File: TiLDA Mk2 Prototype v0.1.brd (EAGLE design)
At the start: 67.9 x 100 mm, 199 parts, among them IC1 ATSAM3X8EA-AU, IC10 MCP73831, IC2 MPU-6050, IC3 SRF-V1.2, IC5 S25FL216K0PMFI011, IC7 HMC5883LSMD (NP), IC8 MCP1825T-3302E/DC, IC9 TC1015-3V3, J1 ZX62-AB-5PA(11), J3 Arduino Headers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

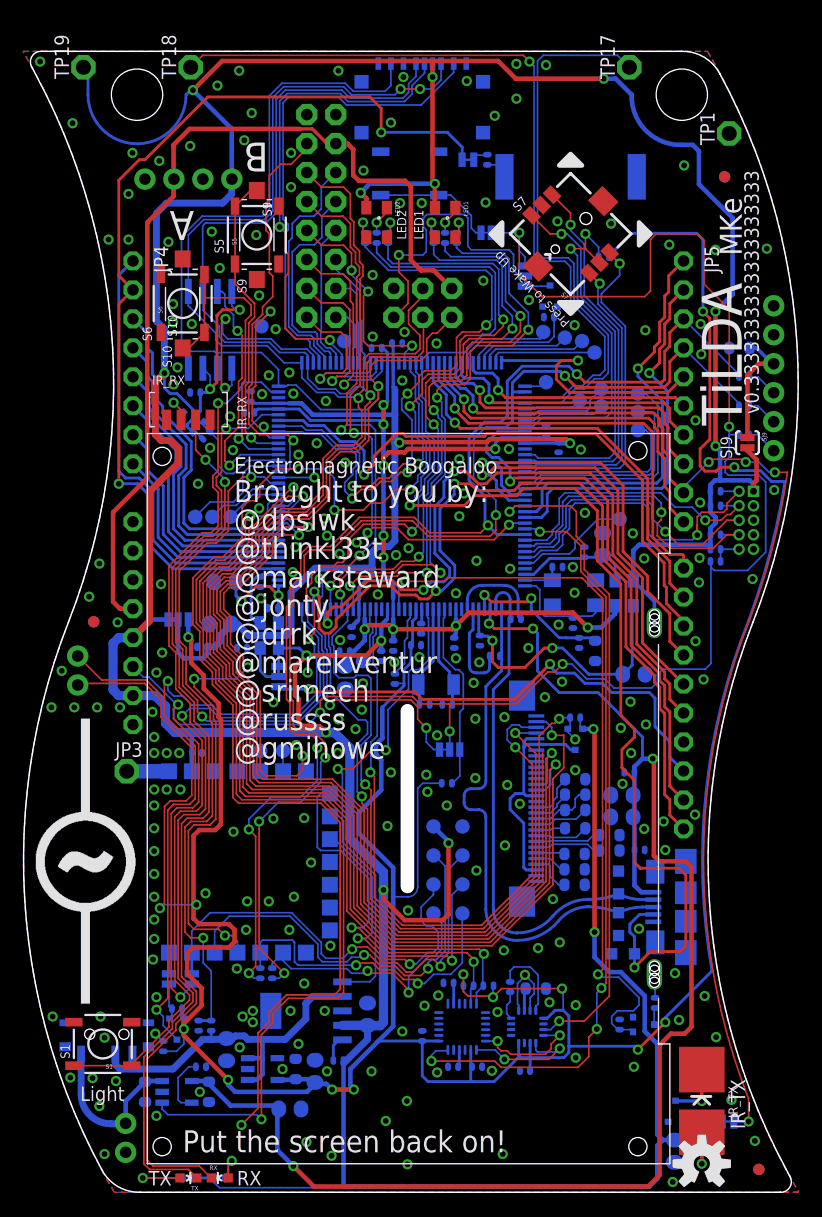
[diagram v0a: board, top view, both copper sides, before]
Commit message: Prototype: Curve all the tracks
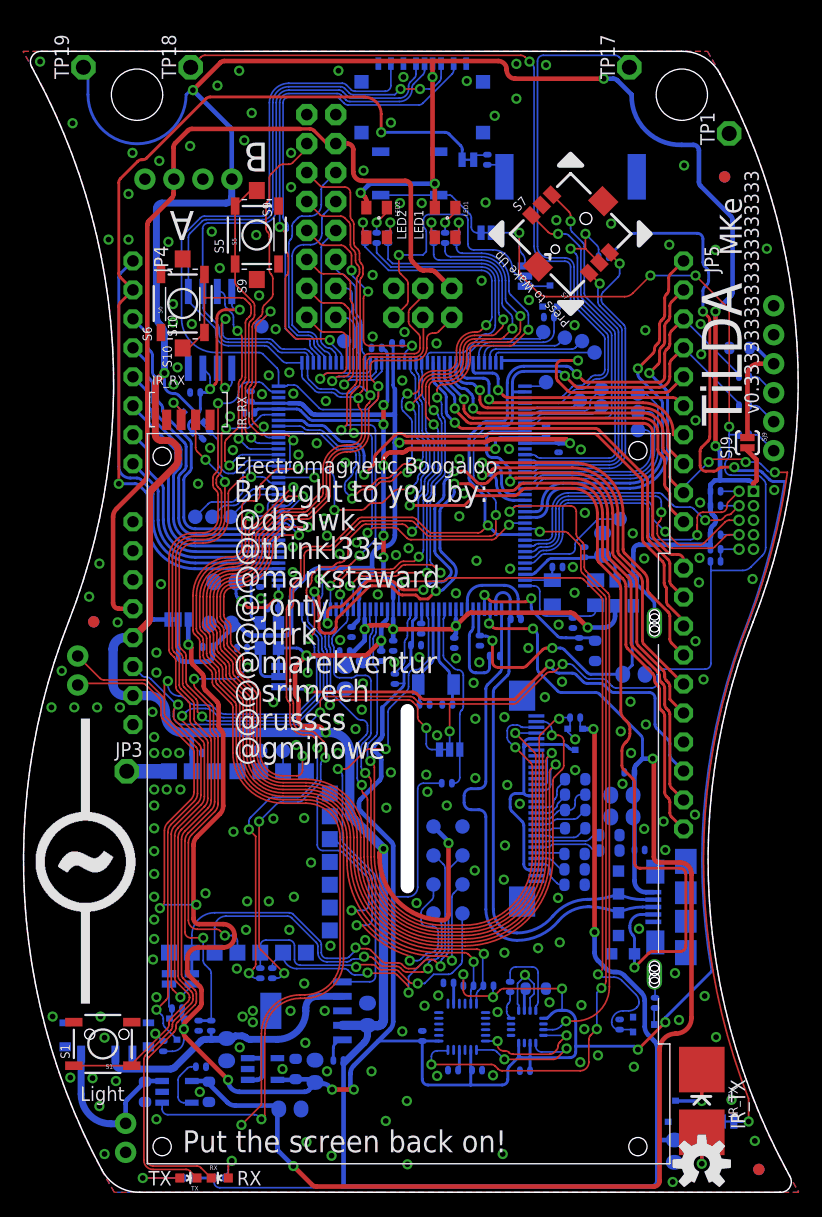
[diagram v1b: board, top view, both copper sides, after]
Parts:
- moved C118 0.50 mm to (16.2, 47.8)
- moved C6 0.30 mm to (37.7, 10.7)
- moved C8 0.30 mm to (39.8, 10.7)
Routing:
- net MASTER_RESET: track 172.9 -> 162.6 mm, vias 7 -> 9
- net MISO: track 169.4 -> 159.6 mm
- net SCK: track 167.6 -> 158.3 mm
- net MOSI: track 172.6 -> 163.3 mm
- net LCD_CS: track 93.9 -> 85.9 mm
- net UOTGVBOF: track 104.8 -> 98.3 mm
- net SCL0-3: track 70.0 -> 63.8 mm
- net SDA0-3: track 71.1 -> 64.9 mm
- net MCP_STAT: track 83.4 -> 77.3 mm
- net LCD_POWER: track 64.6 -> 60.7 mm
- net LCD_A0: track 62.4 -> 58.8 mm
- net LCD_!RST: track 59.0 -> 55.9 mm
- net CANRX0: track 33.5 -> 30.8 mm
- net LED1_GREEN: track 53.4 -> 50.8 mm
- net LED2_GREEN: track 53.3 -> 50.8 mm
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
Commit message: Prototype: more curves
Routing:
- net VBUS: track 124.7 -> 122.9 mm
- net RX: track 109.3 -> 108.1 mm
- net AREF: track 43.2 -> 42.0 mm
- net TX: track 105.1 -> 103.9 mm
- net 3V3: track 522.5 -> 521.4 mm
- net ERASE_S: track 97.2 -> 96.2 mm
- net LIGHT: track 62.9 -> 61.9 mm
- net 5V0: track 79.6 -> 78.7 mm
- net VBACKUP: track 313.5 -> 312.7 mm
- net MOSI: track 163.3 -> 162.5 mm
- net DAC0: track 82.8 -> 82.0 mm
- net RXD2: track 68.6 -> 67.9 mm
- net TXD2: track 47.4 -> 46.7 mm
- net IR_RX: track 49.9 -> 49.2 mm
- net SCK: track 158.3 -> 157.6 mm

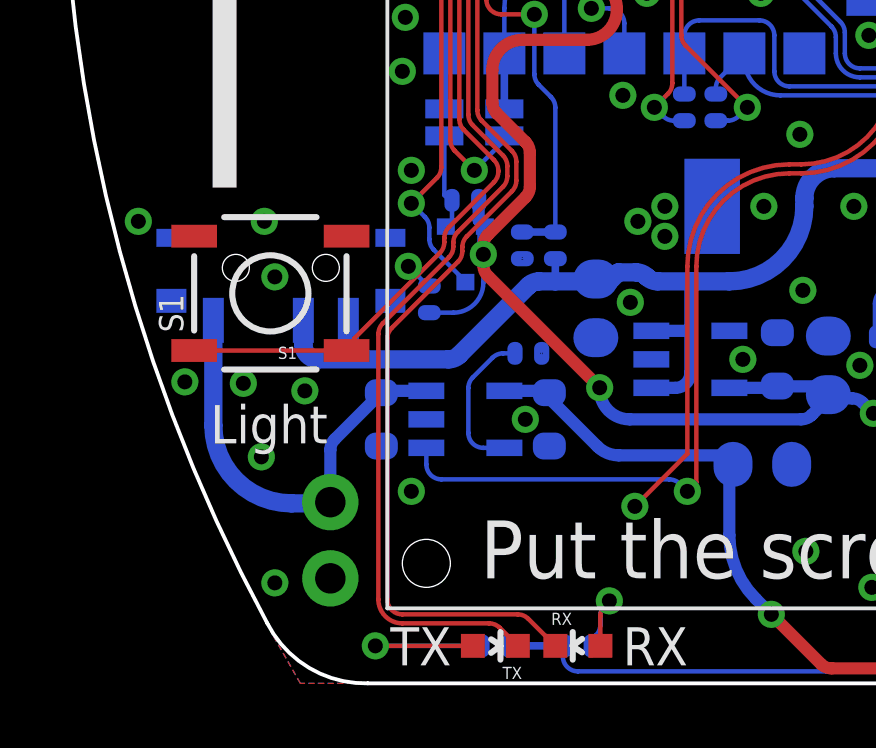
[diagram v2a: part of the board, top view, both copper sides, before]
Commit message: Prototype: Allow power from just USB
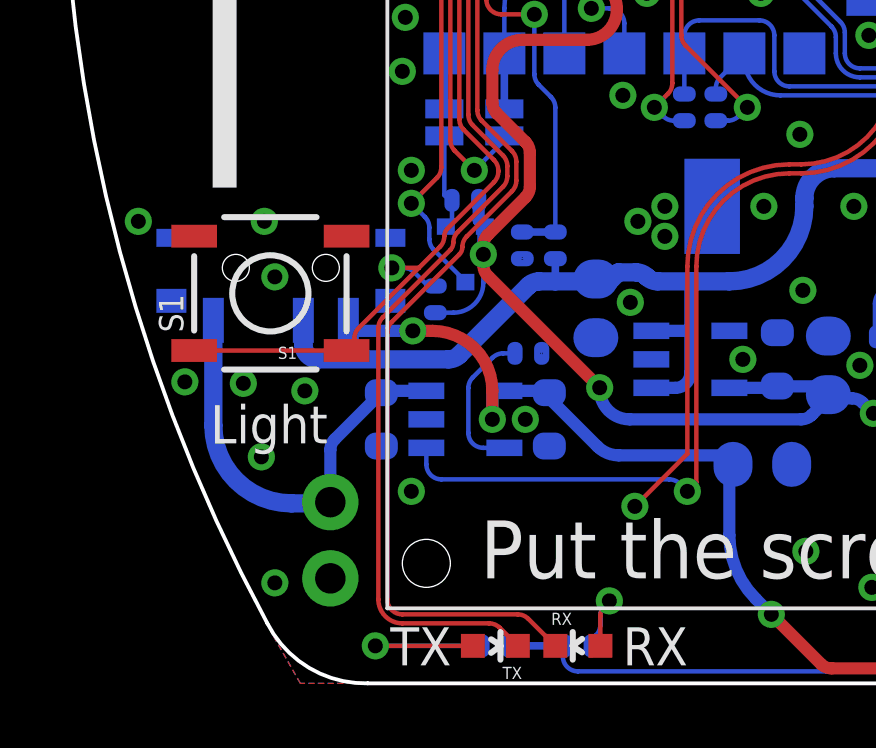
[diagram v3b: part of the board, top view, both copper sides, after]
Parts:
- moved R47 0.20 mm to (12.5, 12.8)
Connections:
- removed net 4V2: S8.1
- net VBUS: now also S8.1
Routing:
- net VBUS: track 122.9 -> 131.1 mm, vias 4 -> 6
- net LIGHT: track 61.9 -> 63.1 mm
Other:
- board text added: "Off/USB"
- board text added: "On/Battery"
- board text removed: "Off On"
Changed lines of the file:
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@@
 <grid distance="0.1" unitdist="mm" unit="mm" style="lines" multiple="1" display="yes" altdistance="0.05" altunitdist="mm" altunit="mm"/>
 <layers>
-<layer number="1" name="Top" color="4" fill="1" visible="no" active="yes"/>
+<layer number="1" name="Top" color="4" fill="1" visible="yes" active="yes"/>
 <layer number="2" name="Route2" color="1" fill="3" visible="no" active="yes"/>
 <layer number="3" name="Route3" color="4" fill="3" visible="no" active="no"/>
@@
 <layer number="21" name="tPlace" color="7" fill="1" visible="no" active="yes"/>
 <layer number="22" name="bPlace" color="6" fill="1" visible="yes" active="yes"/>
-<layer number="23" name="tOrigins" color="15" fill="1" visible="no" active="yes"/>
+<layer number="23" name="tOrigins" color="15" fill="1" visible="yes" active="yes"/>
 <layer number="24" name="bOrigins" color="15" fill="1" visible="yes" active="yes"/>
 <layer number="25" name="tNames" color="7" fill="1" visible="no" active="yes"/>
@@
 <text x="38.9" y="74.6" size="0.6096" layer="22" font="vector" ratio="15" rot="MR0">C108</text>
 <text x="55.2" y="30.65" size="0.6096" layer="22" font="vector" ratio="15" rot="MR0">C126</text>
-<text x="9.6" y="16.8" size="0.8128" layer="22" font="vector" ratio="15" rot="MR0">Off  On</text>
+<text x="8.4" y="16.7" size="0.8128" layer="22" font="vector" ratio="15" rot="MR90">Off/USB</text>
 <text x="7.2" y="11.5" size="0.8128" layer="22" font="vector" ratio="15" rot="MR0">S8</text>
 <text x="63" y="90.7" size="0.8128" layer="22" font="vector" ratio="15" rot="MR0">GND</text>
@@
 <text x="41.5" y="52.5" size="0.8128" layer="22" font="vector" ratio="15" rot="MR45">You did not see this. Tell no one.</text>
 <text x="18.5" y="38" size="1.9304" layer="21" font="vector" ratio="15">@gmjhowe</text>
+<text x="5.5" y="16.8" size="0.8128" layer="22" font="vector" ratio="15" rot="MR90">On/Battery</text>
 </plain>
 <attributes>
@@
 </element>
 <element name="J6" library="TiLDA Mk2 Parts" package="POWER-POD-EMF" value="B016 - PowerPOD NCP1402 5V0" x="14.5" y="88.8" rot="MR0"/>
-<element name="R47" library="TiLDA Mk2 Parts" package="R0402-ARDUINO-ROUND" value="0402/10K/5%" x="12.3" y="12.8" rot="MR270"/>
+<element name="R47" library="TiLDA Mk2 Parts" package="R0402-ARDUINO-ROUND" value="0402/10K/5%" x="12.5" y="12.8" rot="MR270"/>
 <element name="R48" library="TiLDA Mk2 Parts" package="R0402-ARDUINO-ROUND" value="0402/10K/5%" x="50.9" y="82" rot="MR180"/>
 <element name="C50" library="TiLDA Mk2 Parts" package="C0805RNDPOL" value="0805/10u/6V3/X5R" x="25.6" y="10.6" rot="MR90"/>
@@
 <via x="50.4" y="12" extent="1-16" drill="0.5"/>
 <via x="48.85" y="11.4" extent="1-16" drill="0.5"/>
+<wire x1="15.4" y1="14.1555" x2="16.0445" y2="11" width="0" layer="19" extent="16-16"/>
 </signal>
 <signal name="LCD_CS">
@@
 <wire x1="15.24289375" y1="2.3" x2="11.4" y2="2.3" width="0.15" layer="1"/>
 <wire x1="11.4" y1="2.3" x2="10.9" y2="2.8" width="0.15" layer="1" curve="-90"/>
-<wire x1="10.9" y1="2.8" x2="10.9" y2="11.49289375" width="0.15" layer="1"/>
-<wire x1="10.9" y1="11.49289375" x2="11.046446875" y2="11.846446875" width="0.15" layer="1" curve="-45"/>
-<wire x1="11.046446875" y1="11.846446875" x2="13.253553125" y2="14.053553125" width="0.15" layer="1"/>
-<wire x1="13.253553125" y1="14.053553125" x2="13.4" y2="14.40710625" width="0.15" layer="1" curve="45"/>
-<wire x1="13.4" y1="14.40710625" x2="13.4" y2="14.54289375" width="0.15" layer="1"/>
+<wire x1="10.9" y1="2.8" x2="10.9" y2="11.69289375" width="0.15" layer="1"/>
+<wire x1="10.9" y1="11.69289375" x2="11.046446875" y2="12.046446875" width="0.15" layer="1" curve="-45"/>
+<wire x1="11.046446875" y1="12.046446875" x2="13.298959375" y2="14.298959375" width="0.15" layer="1"/>
+<wire x1="13.298959375" y1="14.298959375" x2="13.4" y2="14.54289375" width="0.15" layer="1" curve="45"/>
 <wire x1="13.4" y1="14.54289375" x2="13.546446875" y2="14.896446875" width="0.15" layer="1" curve="-45"/>
 <wire x1="13.546446875" y1="14.896446875" x2="15.053553125" y2="16.403553125" width="0.15" layer="1"/>
@@
 <wire x1="14.9" y1="17.24289375" x2="14.9" y2="16.90710625" width="0.15" layer="1"/>
 <wire x1="14.9" y1="16.90710625" x2="14.753553125" y2="16.553553125" width="0.15" layer="1" curve="-45"/>
-<wire x1="13.1" y1="14.55710625" x2="13.1" y2="14.69289375" width="0.15" layer="1"/>
+<wire x1="10.6" y1="2.8" x2="10.6" y2="11.84289375" width="0.15" layer="1"/>
+<wire x1="10.6" y1="11.84289375" x2="10.746446875" y2="12.196446875" width="0.15" layer="1" curve="-45"/>
+<wire x1="10.746446875" y1="12.196446875" x2="12.998959375" y2="14.448959375" width="0.15" layer="1"/>
+<wire x1="12.998959375" y1="14.448959375" x2="13.1" y2="14.69289375" width="0.15" layer="1" curve="45"/>
 <wire x1="13.1" y1="14.69289375" x2="13.246446875" y2="15.046446875" width="0.15" layer="1" curve="-45"/>
 <wire x1="13.246446875" y1="15.046446875" x2="14.753553125" y2="16.553553125" width="0.15" layer="1"/>
@@
 <wire x1="14.29289375" y1="2" x2="11.4" y2="2" width="0.15" layer="1"/>
 <wire x1="11.4" y1="2" x2="10.6" y2="2.8" width="0.15" layer="1" curve="-90"/>
-<wire x1="10.6" y1="2.8" x2="10.6" y2="11.64289375" width="0.15" layer="1"/>
-<wire x1="10.6" y1="11.64289375" x2="10.746446875" y2="11.996446875" width="0.15" layer="1" curve="-45"/>
-<wire x1="10.746446875" y1="11.996446875" x2="12.953553125" y2="14.203553125" width="0.15" layer="1"/>
-<wire x1="12.953553125" y1="14.203553125" x2="13.1" y2="14.55710625" width="0.15" layer="1" curve="45"/>
 <wire x1="22.4" y1="70.15" x2="21.95710625" y2="70.15" width="0.15" layer="16"/>
 <wire x1="21.95710625" y1="70.15" x2="21.603553125" y2="70.296446875" width="0.15" layer="16" curve="-45"/>
@@
 <wire x1="22.423" y1="7.3" x2="22.35" y2="7.3" width="0.4064" layer="16"/>
 <wire x1="22.35" y1="7.3" x2="22.05" y2="7.6" width="0.4064" layer="16"/>
+<contactref element="S8" pad="1"/>
+<wire x1="9.6" y1="12.1" x2="9.6" y2="11.75" width="0.4064" layer="16"/>
+<wire x1="9.6" y1="11.75" x2="11.75" y2="11.75" width="0.4064" layer="16"/>
+<via x="11.75" y="11.75" extent="1-16" drill="0.5"/>
+<wire x1="11.75" y1="11.75" x2="12.4" y2="11.75" width="0.4064" layer="1"/>
+<wire x1="12.4" y1="11.75" x2="14.4" y2="9.75" width="0.4064" layer="1" curve="-90"/>
+<wire x1="14.4" y1="9.75" x2="14.4" y2="8.8" width="0.4064" layer="1"/>
+<via x="14.4" y="8.8" extent="1-16" drill="0.5"/>
+<wire x1="14.4" y1="8.8" x2="14.4" y2="9.75" width="0.4064" layer="16"/>
+<wire x1="14.4" y1="9.75" x2="14.8" y2="9.75" width="0.4064" layer="16"/>
+<wire x1="14.8" y1="9.75" x2="14.8001" y2="9.75" width="0" layer="19" extent="16-16"/>
 </signal>
 <signal name="JTAG_RESET">
@@
 <wire x1="9.54" y1="11.095" x2="4.46" y2="11.095" width="0.15" layer="1"/>
 <contactref element="IC1" pad="72"/>
-<wire x1="9.8" y1="11.1" x2="9.8" y2="11.5" width="0.15" layer="1"/>
-<wire x1="9.8" y1="11.5" x2="11.9" y2="13.6" width="0.15" layer="1"/>
-<wire x1="11.9" y1="13.6" x2="12.653553125" y2="14.353553125" width="0.15" layer="1"/>
-<wire x1="12.653553125" y1="14.353553125" x2="12.8" y2="14.70710625" width="0.15" layer="1" curve="45"/>
-<wire x1="12.8" y1="14.70710625" x2="12.8" y2="14.84289375" width="0.15" layer="1"/>
-<wire x1="12.8" y1="14.84289375" x2="12.946446875" y2="15.196446875" width="0.15" layer="1" curve="-45"/>
-<wire x1="12.946446875" y1="15.196446875" x2="14.453553125" y2="16.703553125" width="0.15" layer="1"/>
+<wire x1="9.8" y1="11.1" x2="9.8" y2="11.49289375" width="0.15" layer="1"/>
+<wire x1="9.8" y1="11.49289375" x2="9.946446875" y2="11.846446875" width="0.15" layer="1" curve="-45"/>
+<wire x1="9.946446875" y1="11.846446875" x2="11.95" y2="13.85" width="0.15" layer="1"/>
+<wire x1="11.95" y1="13.85" x2="12.653553125" y2="14.553553125" width="0.15" layer="1"/>
+<wire x1="12.653553125" y1="14.553553125" x2="12.8" y2="14.90710625" width="0.15" layer="1" curve="45"/>
+<wire x1="12.8" y1="14.90710625" x2="12.901040625" y2="15.151040625" width="0.15" layer="1" curve="-45"/>
+<wire x1="12.901040625" y1="15.151040625" x2="14.453553125" y2="16.703553125" width="0.15" layer="1"/>
 <wire x1="14.453553125" y1="16.703553125" x2="14.6" y2="17.05710625" width="0.15" layer="1" curve="45"/>
 <wire x1="14.6" y1="17.05710625" x2="14.6" y2="17.09289375" width="0.15" layer="1"/>
@@
 <via x="13.95" y="41.75" extent="1-16" drill="0.5"/>
 <contactref element="R47" pad="1"/>
-<wire x1="12.3" y1="13.2445" x2="12.2555" y2="13.2445" width="0.15" layer="16"/>
-<wire x1="12.2555" y1="13.2445" x2="11.6" y2="13.9" width="0.15" layer="16"/>
-<via x="11.6" y="13.9" extent="1-16" drill="0.5"/>
-<wire x1="11.6" y1="13.9" x2="11.9" y2="13.6" width="0.15" layer="1"/>
+<wire x1="12.5" y1="13.2445" x2="12.2555" y2="13.2445" width="0.15" layer="16"/>
+<wire x1="12.2555" y1="13.2445" x2="11.796446875" y2="13.703553125" width="0.15" layer="16"/>
+<wire x1="11.796446875" y1="13.703553125" x2="11.44289375" y2="13.85" width="0.15" layer="16" curve="45"/>
+<wire x1="11.44289375" y1="13.85" x2="11.05" y2="13.85" width="0.15" layer="16"/>
+<via x="11.05" y="13.85" extent="1-16" drill="0.5"/>
+<wire x1="11.05" y1="13.85" x2="11.95" y2="13.85" width="0.15" layer="1"/>
 </signal>
 <signal name="N$8">
@@
 <contactref element="R47" pad="2"/>
 <contactref element="R48" pad="2"/>
-<wire x1="12.3" y1="12.3555" x2="13.1" y2="12.3555" width="0.15" layer="16"/>
+<wire x1="12.5" y1="12.3555" x2="13.1" y2="12.3555" width="0.15" layer="16"/>
 <wire x1="13.1" y1="12.3555" x2="14.1" y2="13.3555" width="0.15" layer="16" curve="90"/>
 <wire x1="14.1" y1="13.3555" x2="14.1" y2="14.3" width="0.15" layer="16"/>
@@
 <wire x1="65.595146875" y1="72.704853125" x2="65.8" y2="72.62" width="0.3084" layer="16" curve="45"/>
 </signal>
-<signal name="4V2">
-<contactref element="S8" pad="1"/>
-</signal>
 <signal name="IR_RX_PWR">

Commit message: Prototype: Even more curves
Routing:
- net PC11: track 35.2 -> 34.7 mm
